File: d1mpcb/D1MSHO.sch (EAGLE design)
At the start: 11 parts, among them T1 BD139

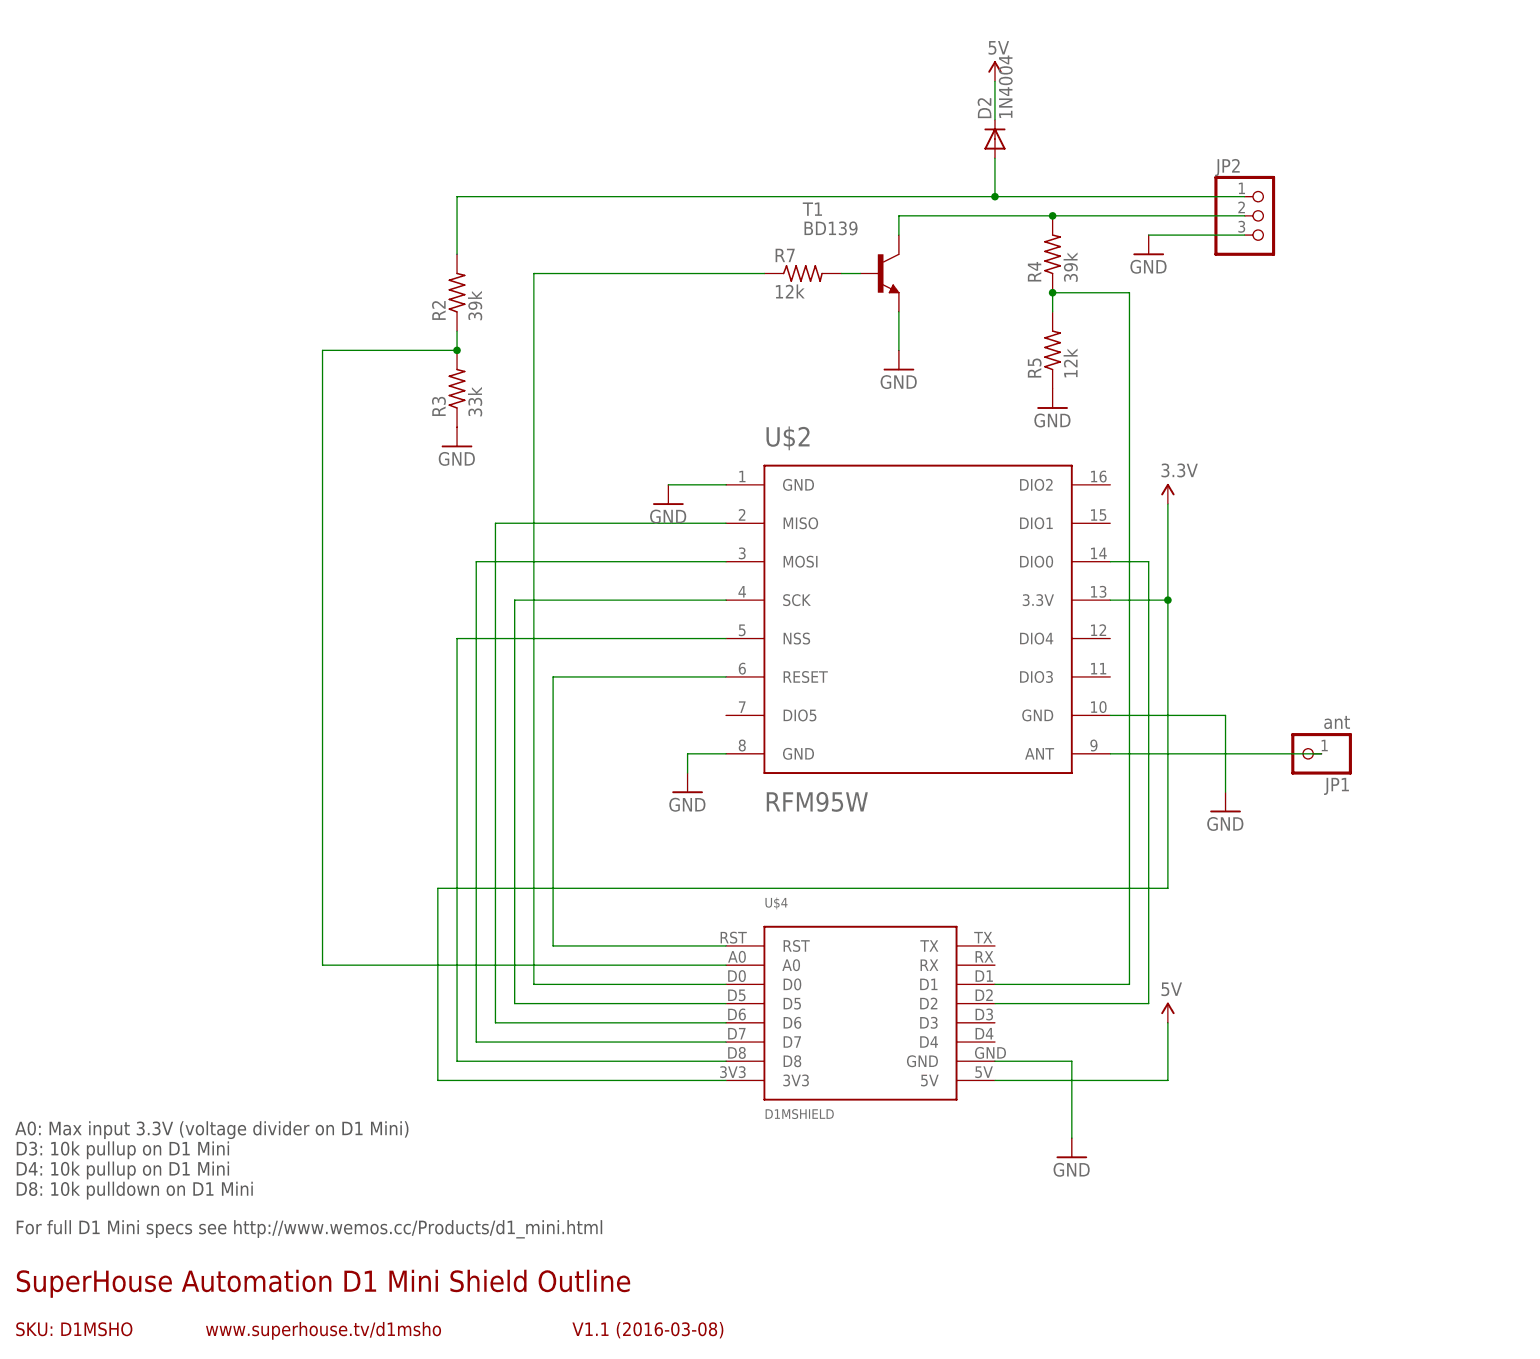
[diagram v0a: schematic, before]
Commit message: new schematic and rx driver
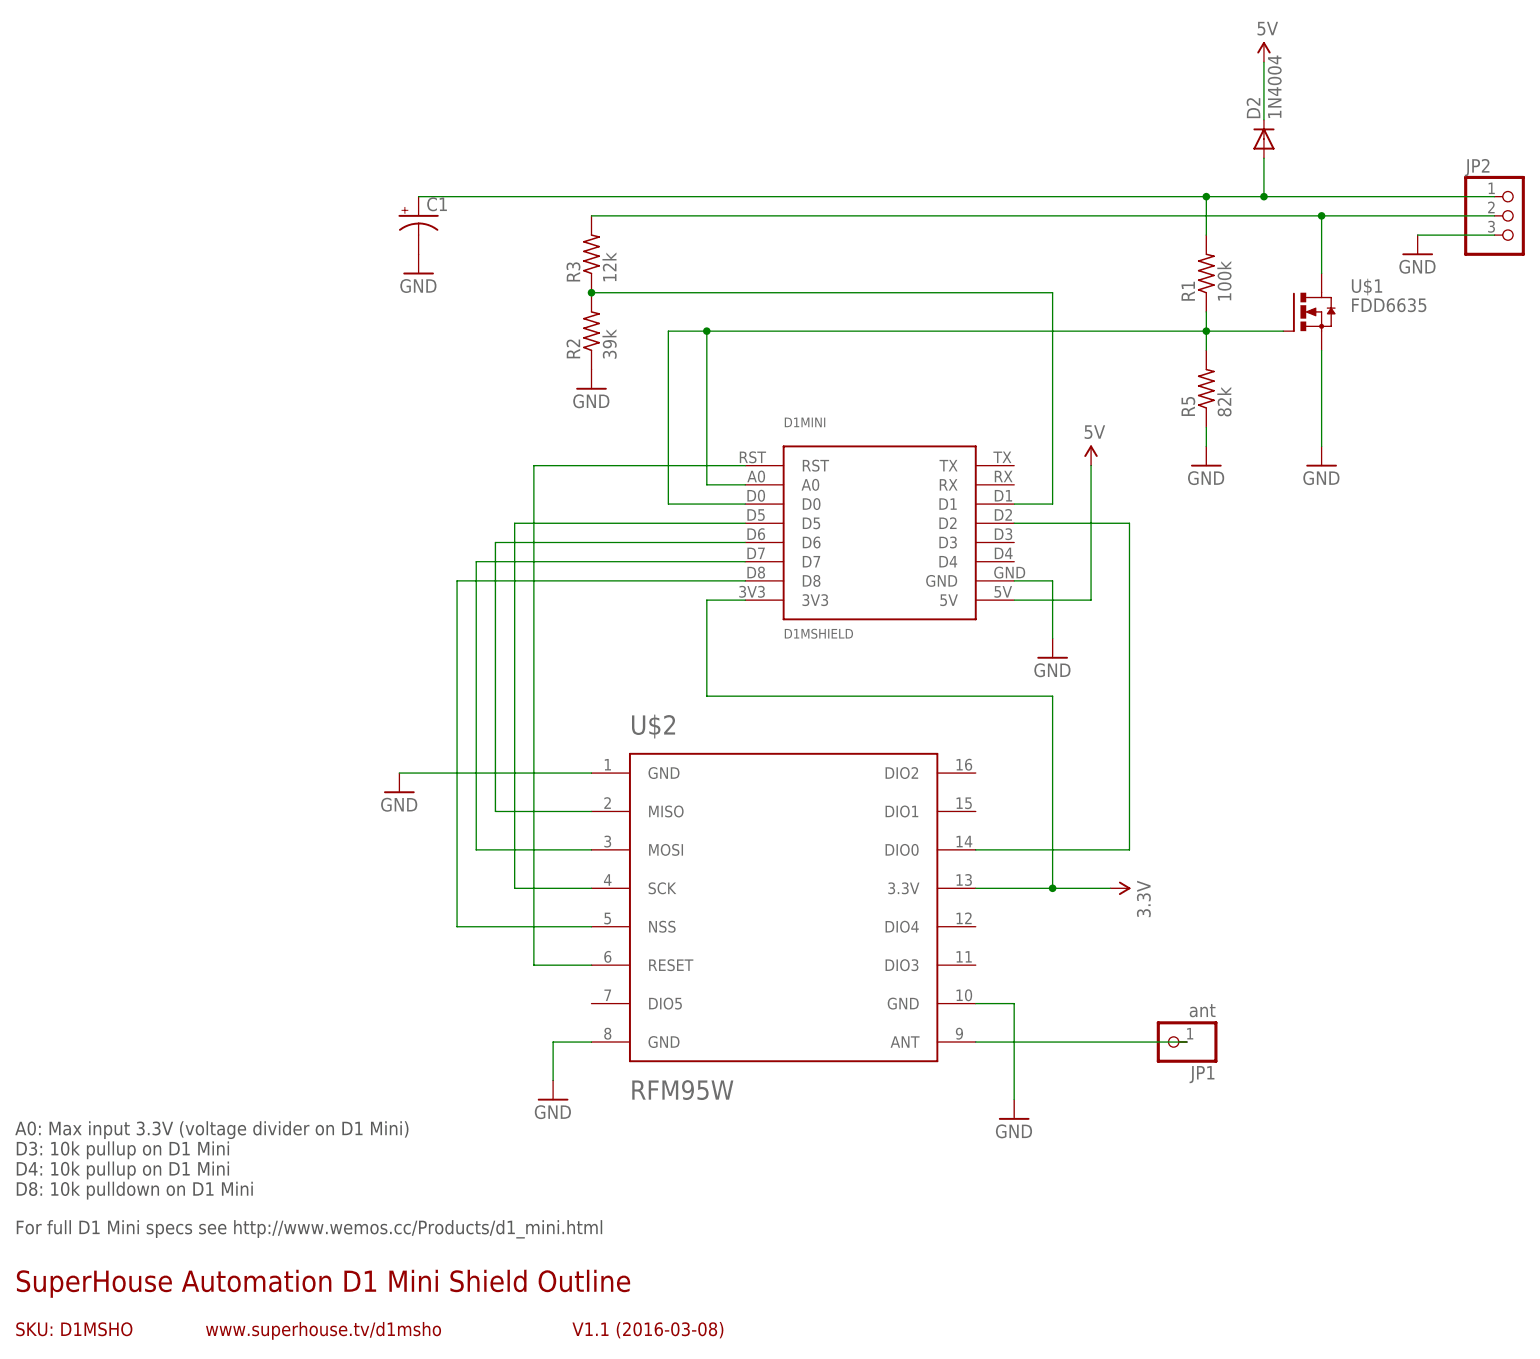
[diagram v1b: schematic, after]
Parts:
- removed R4: 39k, resistor:R-US_M0805
- removed R7: 12k, resistor:R-US_M0805
- removed T1: BD139, transistor:BD139
- removed U$4: D1MSHIELD, d1mshield:D1MSHIELD
- added C1: (no value), resistor:CPOL-USE3.5-8
- added D1MINI: D1MSHIELD, d1mshield:D1MSHIELD
- added R1: 100k, resistor:R-US_M0805
- added U$1: FDD6635, fdd6635:FDD6635
- R3: value 33k -> 12k
- R5: value 12k -> 82k
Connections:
- removed net D0: R7.1, U$4.D0
- removed net D1: R4.1, R5.2, U$4.D1
- net 3.3V: now also D1MINI.3V3; no longer U$4.3V3
- net 5V: now also D1MINI.5V; no longer U$4.5V
- net A0: now also D1MINI.A0, D1MINI.D0, R1.1, R5.2, U$1.G; no longer R2.1, R3.2, U$4.A0
- net D5: now also D1MINI.D5; no longer U$4.D5
- net D6: now also D1MINI.D6; no longer U$4.D6
- net D7: now also D1MINI.D7; no longer U$4.D7
- net D8: now also D1MINI.D8; no longer U$4.D8
- net GND: now also C1.-, D1MINI.GND, R2.1, U$1.S; no longer R3.1, T1.E, U$4.GND
- net N$1: now also R3.2, U$1.D; no longer R4.2, T1.C
- net N$2: now also D1MINI.D1, R2.2, R3.1; no longer R7.2, T1.B
- net N$3: now also C1.+, R1.2; no longer R2.2
- net N$6: now also D1MINI.D2; no longer U$4.D2
- net RST: now also D1MINI.RST; no longer U$4.RST
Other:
- moved on the sheet: D2, JP1, JP2, R2, R3, R5, U$2
